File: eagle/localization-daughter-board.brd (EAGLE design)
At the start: 65 x 30 mm, 22 parts, among them U1 LM340MP-5.0/NOPB, U2 RPI-ZERO, U3 LMS8117AMP-ADJ/NOPB, U4 TXS0101DCKR, U5 SN65HVD256DR, U6 STM32F042FXP

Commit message: Finished board
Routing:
- net GND: track 0.00 -> 8.23 mm, vias 0 -> 2
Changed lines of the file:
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@@
 <setting verticaltext="up"/>
 </settings>
-<grid distance="50" unitdist="mil" unit="mil" style="lines" multiple="1" display="yes" altdistance="1" altunitdist="mil" altunit="mil"/>
+<grid distance="50" unitdist="mil" unit="mil" style="lines" multiple="1" display="yes" altdistance="25" altunitdist="mil" altunit="mil"/>
 <layers>
 <layer number="1" name="Top" color="4" fill="1" visible="yes" active="yes"/>
@@
 <contactref element="C7" pad="2"/>
 <contactref element="C4" pad="2"/>
+<via x="8.89" y="10.16" extent="1-16" drill="0.55" diameter="1.05"/>
+<via x="13.97" y="8.89" extent="1-16" drill="0.55" diameter="1.05"/>
+<wire x1="8.89" y1="10.16" x2="12.7" y2="10.16" width="1.27" layer="16"/>
+<wire x1="12.7" y1="10.16" x2="13.97" y2="8.89" width="1.27" layer="16"/>
+<wire x1="10.16" y1="5.72658125" x2="10.16" y2="6.6421" width="0.4064" layer="1"/>
+<wire x1="10.16" y1="6.6421" x2="10.3274" y2="6.8095" width="0.3048" layer="1"/>
+<wire x1="10.3274" y1="6.8095" x2="10.3274" y2="7.35255" width="0.3048" layer="1"/>
+<wire x1="10.3274" y1="7.35255" x2="10.59485" y2="7.62" width="0.3048" layer="1"/>
+<wire x1="10.59485" y1="7.62" x2="11.14131875" y2="7.62" width="0.3048" layer="1"/>
 </signal>
 <signal name="+12V">

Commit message: Updated schematic and BOM
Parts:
- C5: value 100nF -> 0.1u
- R1: value (none) -> 47k
- R2: value (none) -> 9.53k
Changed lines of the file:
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@@
 <attribute name="NAME" x="7.3378" y="17.3162" size="1.27" layer="25"/>
 </element>
-<element name="C5" library="resistor" library_urn="urn:adsk.eagle:library:348" package="C0805" package3d_urn="urn:adsk.eagle:package:26137/1" value="100nF" x="10.16" y="21.59" smashed="yes" rot="R90">
+<element name="C5" library="resistor" library_urn="urn:adsk.eagle:library:348" package="C0805" package3d_urn="urn:adsk.eagle:package:26137/1" value="0.1u" x="10.16" y="21.59" smashed="yes" rot="R90">
 <attribute name="NAME" x="10.2108" y="18.034" size="1.27" layer="25"/>
 </element>
@@
 <attribute name="VENDOR" value="Texas Instruments" x="41.91" y="13.97" size="1.778" layer="27" rot="R90" display="off"/>
 </element>
-<element name="R2" library="resistor" library_urn="urn:adsk.eagle:library:348" package="R0805" package3d_urn="urn:adsk.eagle:package:26059/1" value="" x="36.195" y="15.875" smashed="yes" rot="R90">
+<element name="R2" library="resistor" library_urn="urn:adsk.eagle:library:348" package="R0805" package3d_urn="urn:adsk.eagle:package:26059/1" value="9.53k" x="36.195" y="15.875" smashed="yes" rot="R90">
 <attribute name="NAME" x="32.9438" y="15.1638" size="1.27" layer="25"/>
 <attribute name="VALUE" x="38.735" y="15.24" size="1.27" layer="27" rot="R90"/>
 </element>
-<element name="R1" library="resistor" library_urn="urn:adsk.eagle:library:348" package="R0805" package3d_urn="urn:adsk.eagle:package:26059/1" value="" x="36.195" y="11.43" smashed="yes" rot="R270">
+<element name="R1" library="resistor" library_urn="urn:adsk.eagle:library:348" package="R0805" package3d_urn="urn:adsk.eagle:package:26059/1" value="47k" x="36.195" y="11.43" smashed="yes" rot="R270">
 <attribute name="NAME" x="37.3888" y="8.636" size="1.27" layer="25"/>
 <attribute name="VALUE" x="33.655" y="12.065" size="1.27" layer="27" rot="R270"/>

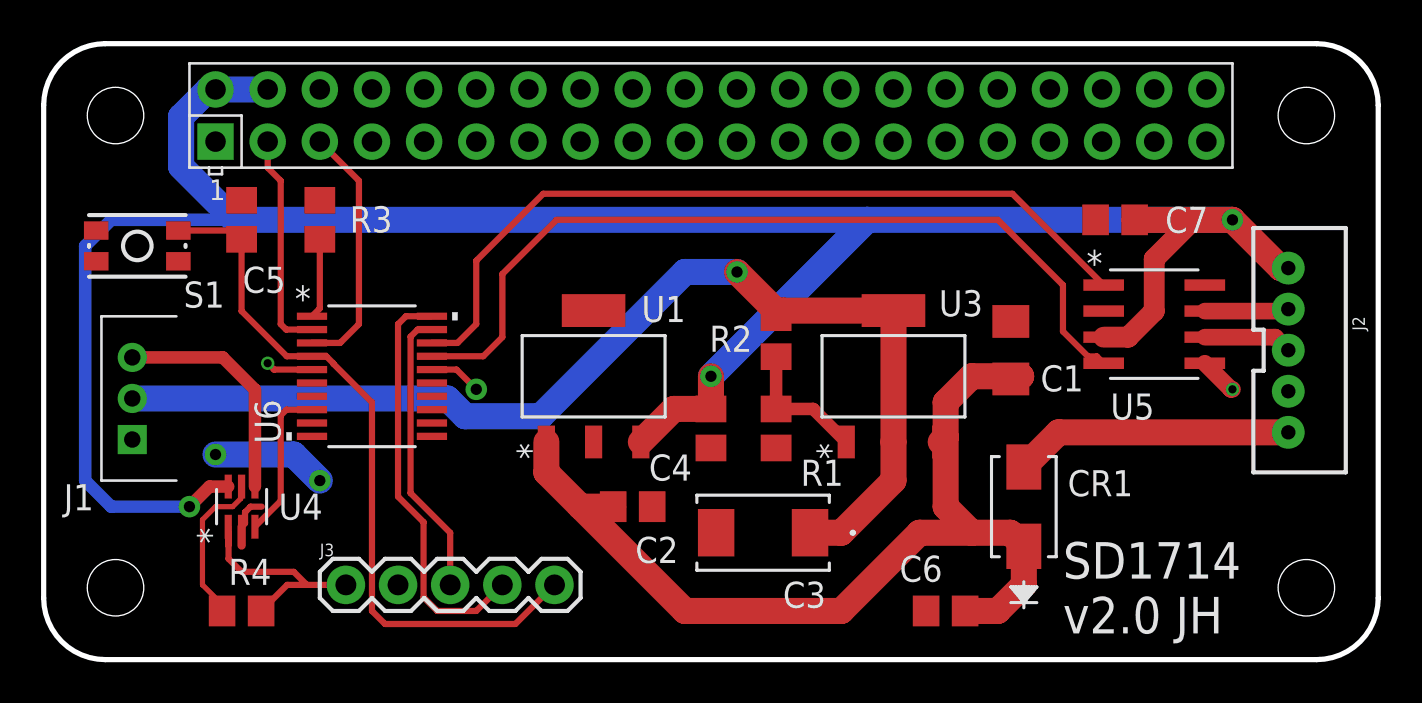
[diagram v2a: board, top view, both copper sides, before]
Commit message: Added most of the new components
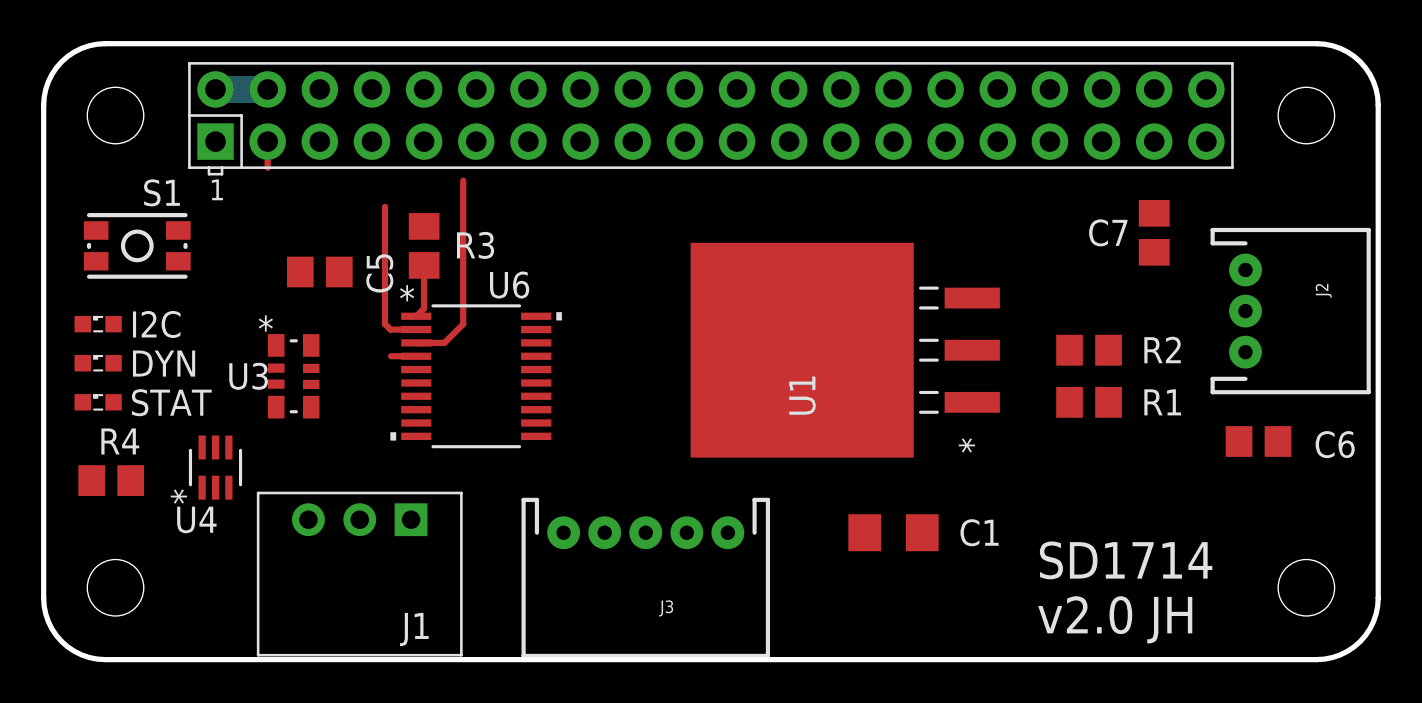
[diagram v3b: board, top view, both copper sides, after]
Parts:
- removed C2: 22u, resistor:C0805
- removed C3: 100u, Localization-Daughter-Board:F93-C
- removed C4: 0.1u, resistor:C0805
- removed CR1: STPS2H100A, Localization-Daughter-Board:SMA
- removed U5: SN65HVD256DR, Localization-Daughter-Board:D8
- added DYN, I2C, STAT: (no value), led:SML0603
- C1: value 10u -> 22u
- J1: value (none) -> MOLEX-22-03-5035; device Localization-Daughter-Board:MOLEX-053253-0370 -> bbb_localization_cape:MOLEX-22-05-7035
- J2: device SparkFun-Connectors:JST-5-PTH-VERT -> SparkFun-Connectors:JST-3-PTH
- J3: device SparkFun-Connectors:1X05 -> SparkFun-Connectors:JST-5-PTH
- R1: value 47k -> 910
- R2: value 9.53k -> 130
- U1: value LM340MP-5.0/NOPB -> LM1085ISX-ADJ; device Localization-Daughter-Board:MP04A -> bbb_localization_cape:TS3B
- U3: value LMS8117AMP-ADJ/NOPB -> EXB-38V121JV; device Localization-Daughter-Board:MP04A -> Localization-Daughter-Board:C_ARRAY_EXB38V
- moved U3 29.2 mm to (12.7, 14.0), turned to 0 degrees
- moved C6 17.3 mm to (59.7, 10.8), turned to 0 degrees
- moved R1 15.3 mm to (51.4, 12.7), turned to 180 degrees
- moved R2 15.3 mm to (51.4, 15.2), turned to 180 degrees
- moved J3 14.8 mm to (29.8, 6.35), turned to 180 degrees
- moved J1 11.6 mm to (18.4, 6.99), turned to 180 degrees
- moved C1 10.6 mm to (41.9, 6.35), turned to 0 degrees
- moved U1 10.2 mm to (37.5, 15.2)
- moved R4 8.98 mm to (3.81, 8.89)
- moved R3 5.24 mm to (19.1, 20.3)
- moved U6 5.08 mm to (21.6, 14.0)
- moved C5 4.58 mm to (14.0, 19.1), turned to 180 degrees
- moved J2 2.69 mm to (59.1, 17.1)
- moved U4 2.29 mm to (8.89, 9.53)
- moved C7 2.01 mm to (54.6, 21.0), turned to 270 degrees
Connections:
- removed net +7V4: C3.1, J1.2, R2.2, U3.2, U3.4
- removed net CAN_RX: U5.4, U6.17
- removed net CAN_TX: U5.1, U6.18
- removed net N$2: J2.2, U5.7
- removed net N$4: R1.1, R2.1, U3.1
- removed net UART_DYN_5V: J1.3, U4.4
- removed net VIN: CR1.2, J2.5
- new net +10V: C1.1, J1.P$2, R2.2, U1.2, U1.4
- new net DYN_DATA: J1.P$3, U4.4
- net +12V: now also J2.3, U1.3; no longer C1.1, C2.1, CR1.1, U1.1, U3.3
- net +3V3: no longer U5.5
- net +5V: no longer C4.1, U1.3, U5.3
- net GND: now also J1.P$1, J2.2, R1.1; no longer C2.2, C3.2, C4.2, J1.1, J2.4, R1.2, U1.2, U1.4, U5.2
- net N$3: now also R1.2, R2.1, U1.1; no longer J2.3, U5.6
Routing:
- net +5V: track 119.7 -> 2.54 mm, vias 3 -> 0
- net +7V4: track 55.0 -> 0.00 mm, vias 1 -> 0
- net +12V: track 48.2 -> 0.00 mm
- net CAN_RX: track 41.5 -> 0.00 mm
- net CAN_TX: track 39.4 -> 0.00 mm
- net NRST: track 35.1 -> 1.23 mm
- net SWCLK: track 20.3 -> 0.00 mm
- net +3V3: track 17.9 -> 0.00 mm, vias 3 -> 0
- net SWDIO: track 14.1 -> 0.00 mm
- net VIN: track 13.6 -> 0.00 mm
- net UART_DYN_5V: track 11.3 -> 0.00 mm
- net GND: track 8.23 -> 0.00 mm, vias 2 -> 0
- net DYN_OE: track 7.73 -> 0.00 mm
- net UART_DYN_3V3: track 7.58 -> 0.00 mm
- net N$4: track 6.63 -> 0.00 mm
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- added copper zone on layer 1, net +10V
- added copper zone on layer 16, net GND
- removed copper zone on layer 16, net +3V3
- removed copper zone on layer 1, net GND

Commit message: Finished layout, need to do final check
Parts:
- added SJ1: (no value), jumper:SJ
- added STAT2: (no value), led:SML0603
- J3: device SparkFun-Connectors:JST-5-PTH -> SparkFun-Connectors:JST-5-PTH-VERT
- moved C6 33.0 mm to (26.7, 10.8)
- moved J2 32.9 mm to (27.9, 6.35), turned to 180 degrees
- moved J3 32.4 mm to (61.0, 15.2), turned to 270 degrees
- moved C7 23.3 mm to (35.6, 7.62), turned to 90 degrees
- moved R1 16.9 mm to (34.9, 16.5), turned to 0 degrees
- moved R4 15.9 mm to (19.7, 10.2)
- moved R2 14.7 mm to (36.8, 14.0), turned to 0 degrees
- moved U1 12.8 mm to (50.2, 14.0), turned to 270 degrees
- moved U4 10.6 mm to (19.1, 12.7), turned to 180 degrees
- moved C1 5.39 mm to (38.1, 10.2), turned to 270 degrees
- moved U6 4.58 mm to (24.1, 17.8)
- moved C5 3.86 mm to (10.2, 19.7), turned to 270 degrees
- moved R3 2.84 mm to (16.5, 21.6), turned to 0 degrees
- moved U3 1.80 mm to (14.0, 15.2), turned to 180 degrees
- renumbered STAT to STAT1
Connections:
- new net DYN_LED: U3.3, U6.7
- new net I2C_LED: U3.4, U6.6
- new net N$2: STAT1.A, U3.7
- new net N$4: DYN.A, U3.6
- new net N$5: I2C.A, U3.5
- new net N$6: STAT2.A, U3.8
- new net PI_NRST: SJ1.2, U2.11
- new net PI_RX: U2.10, U6.17
- new net PI_TX: U2.8, U6.18
- new net STAT_LED: U3.1, U6.10
- new net TRACK_LED: U3.2, U6.9
- net GND: now also DYN.C, I2C.C, STAT1.C, STAT2.C
- net NRST: now also SJ1.1
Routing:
- net +3V3: track 0.00 -> 85.4 mm, vias 0 -> 2
- net +5V: track 2.54 -> 72.7 mm, vias 0 -> 1
- net NRST: track 1.23 -> 70.5 mm, vias 0 -> 2
- net GND: track 0.00 -> 59.4 mm, vias 0 -> 3
- net SWDIO: track 0.00 -> 46.1 mm, vias 0 -> 1
- net SWCLK: track 0.00 -> 42.9 mm, vias 0 -> 1
- net +12V: track 0.00 -> 28.7 mm
- net PI_RX: track 0.00 -> 18.3 mm
- net PI_TX: track 0.00 -> 15.9 mm
- net N$6: track 0.00 -> 10.4 mm
- net N$2: track 0.00 -> 10.1 mm
- net N$4: track 0.00 -> 9.62 mm
- net N$5: track 0.00 -> 9.29 mm
- net DYN_DATA: track 0.00 -> 8.83 mm
- net N$3: track 0.00 -> 8.55 mm
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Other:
- board text added: "SD1714 v2.1 JH"
- board text removed: "SD1714 v2.0 JH"
